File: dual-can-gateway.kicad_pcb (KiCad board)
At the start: 2 copper layers, 101.6 x 88.9 mm, 98 parts, among them J3 Conn_01x02_Pin, Q1 AO3401A, Q2 2N7002, U1 STM32F405RGTx, U2 STM32F405RGTx, U3 ESP32-WROOM-32UE, U4 TJA1044GT-3, U5 TJA1044GT-3, U6 TJA1055T/3, U7 TJA1055T/3, U8 LM2596S-5, U9 AMS1117-3.3

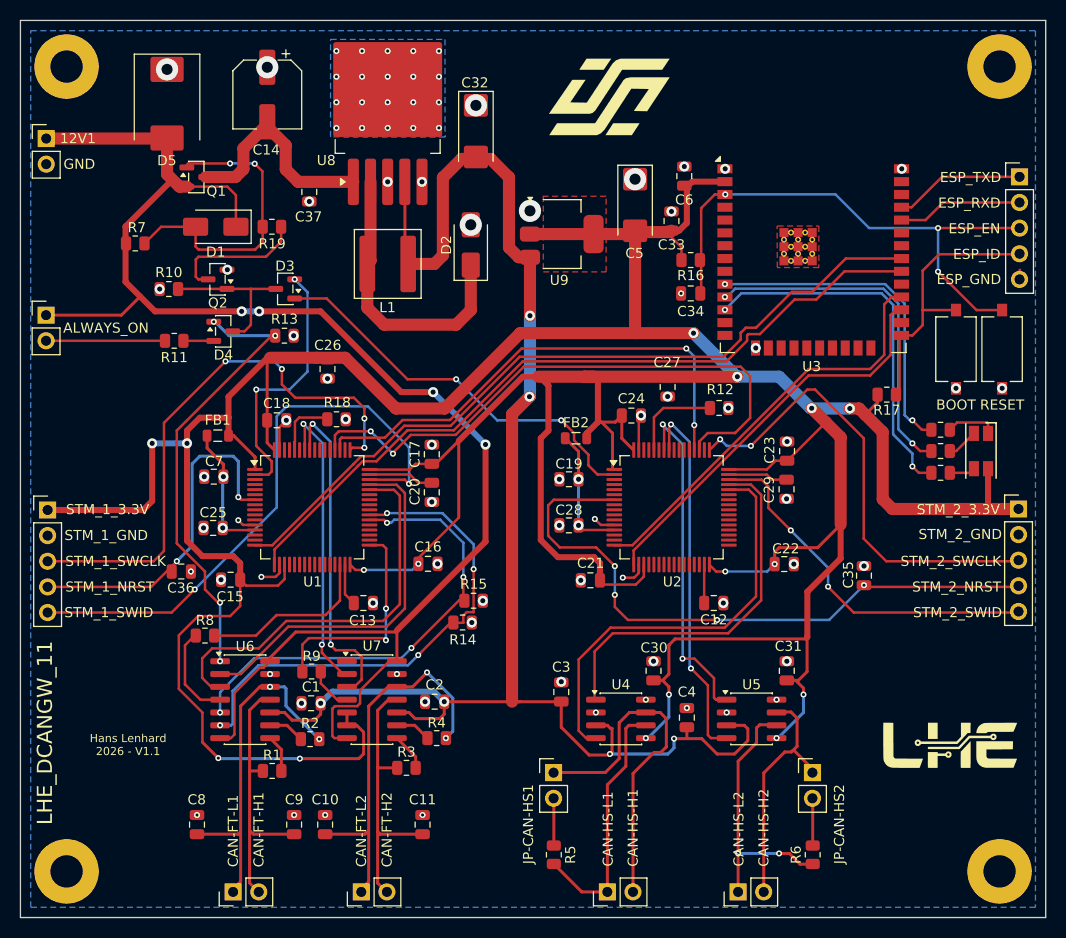
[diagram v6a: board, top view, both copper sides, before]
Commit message: added k-line
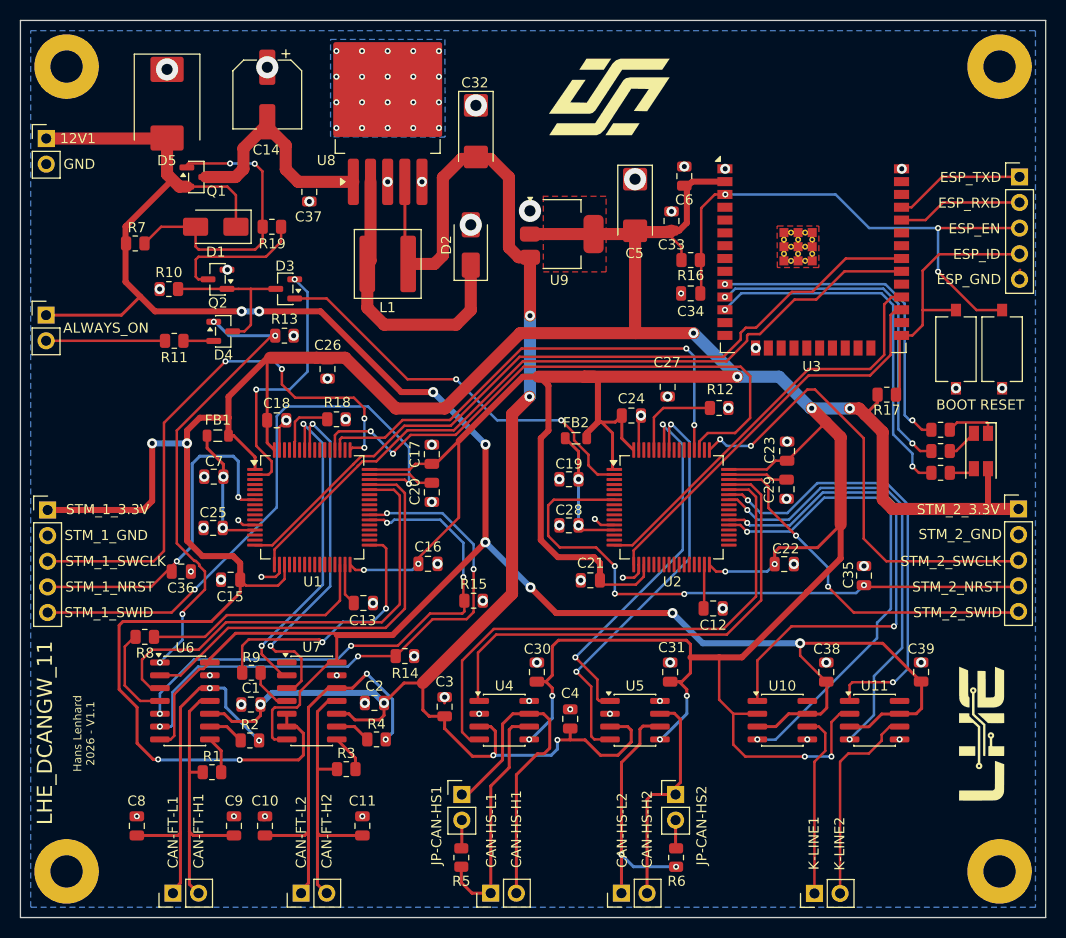
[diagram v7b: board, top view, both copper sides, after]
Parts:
- added C38: 100nf, Capacitor_SMD:C_0805_2012Metric, F.Cu at (92.6, 77.3)
- added C39: 100nf, Capacitor_SMD:C_0805_2012Metric, F.Cu at (102.0, 77.3)
- added K-LINE1: Conn_01x02_Pin, Connector_PinHeader_2.54mm:PinHeader_1x02_P2.54mm_Vertical, F.Cu at (91.4, 99.2)
- added U10: TJA1021xT, Package_SO:SOIC-8_3.9x4.9mm_P1.27mm, F.Cu at (88.2, 82.0)
- added U11: TJA1021xT, Package_SO:SOIC-8_3.9x4.9mm_P1.27mm, F.Cu at (97.3, 82.0)
- moved JP-CAN-HS2 13.7 mm to (77.6, 89.4)
- moved R6 13.5 mm to (77.7, 95.7)
- moved C3 11.6 mm to (54.7, 80.7)
- moved C30 11.6 mm to (63.9, 77.3)
- moved C31 11.6 mm to (77.1, 77.3)
- moved C4 11.6 mm to (67.2, 81.9)
- moved CAN-HS1 11.6 mm to (59.3, 99.2)
- moved CAN-HS2 11.6 mm to (72.3, 99.2)
- moved U5 11.6 mm to (73.6, 82.0)
- moved U4 11.6 mm to (60.6, 82.0)
- moved JP-CAN-HS1 9.35 mm to (56.4, 89.4)
- moved R5 9.17 mm to (56.4, 95.7)
- moved R14 6.61 mm to (50.8, 75.7)
- moved C8 5.97 mm to (24.2, 92.5)
- moved CAN-FT1 5.97 mm to (27.8, 99.2)
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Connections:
- U2 pad 37: unconnected-(U2-PC6-Pad37) -> Net-(U10-TXD)
- U2 pad 38: unconnected-(U2-PC7-Pad38) -> Net-(U10-RXD)
- U2 pad 42: unconnected-(U2-PA9-Pad42) -> Net-(U11-TXD)
- U2 pad 43: unconnected-(U2-PA10-Pad43) -> Net-(U11-RXD)
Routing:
- net /12V_Protected: track 153.9 -> 234.3 mm, vias 4 -> 8
- net Net-(U10-RXD): track 0.00 -> 49.7 mm, vias 0 -> 2
- net Net-(U10-TXD): track 0.00 -> 47.7 mm, vias 0 -> 2
- net Net-(U11-TXD): track 0.00 -> 45.4 mm, vias 0 -> 2
- net Net-(U11-RXD): track 0.00 -> 44.9 mm, vias 0 -> 2
- net /3.3V: track 454.1 -> 496.9 mm, vias 16 -> 18
- net Net-(K-LINE1-Pin_2): track 0.00 -> 20.7 mm
- net Net-(K-LINE1-Pin_1): track 0.00 -> 18.4 mm
- net Net-(U2-PA11): track 42.1 -> 53.7 mm
- net Net-(U2-PA12): track 37.5 -> 49.1 mm
- net Net-(U1-PC7): track 46.1 -> 52.8 mm
- net Net-(U1-PA12): track 36.3 -> 42.3 mm
- net Net-(U1-PB11): track 17.5 -> 23.5 mm
- net Net-(U1-PA11): track 39.9 -> 45.9 mm
- net Net-(U1-PC8): track 50.5 -> 56.1 mm
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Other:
- board text added: "K-LINE2"
